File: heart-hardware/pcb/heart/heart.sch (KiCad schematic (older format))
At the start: 61 parts, among them J1 3V0, J2 DIO, J3 CLK, J4 GND, SW1 SW_SPDT, U1 STM32L031F6Px, U2 TCA6416APWR, U3 LIS3DH

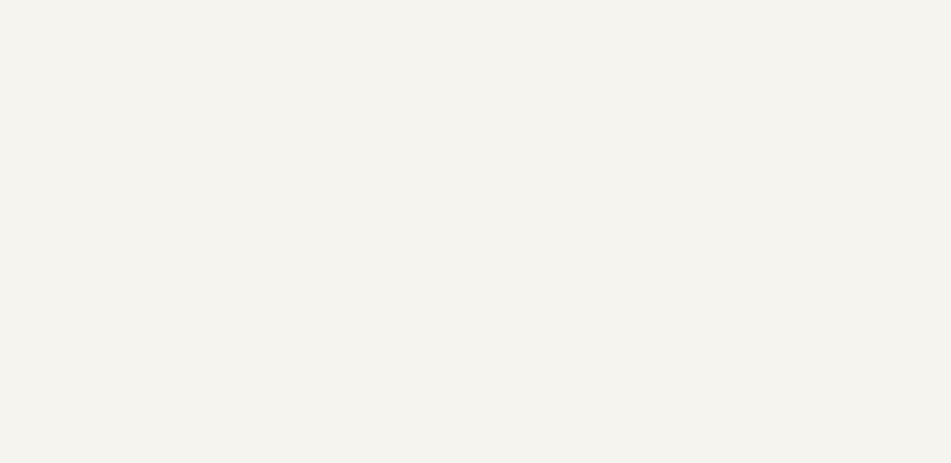
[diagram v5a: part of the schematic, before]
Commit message: Added touch key
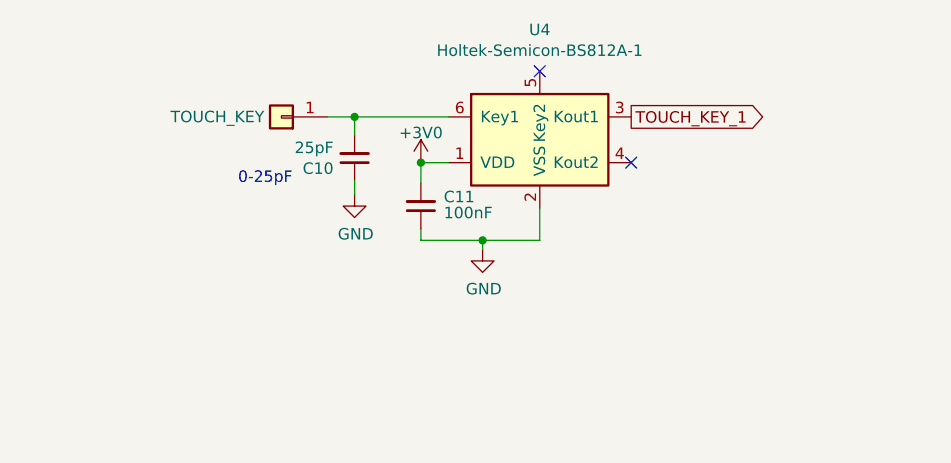
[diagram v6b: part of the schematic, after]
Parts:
- added C10: 25pF, Capacitor_SMD:C_0402_1005Metric, symbol Device:C_Small
- added C11: 100nF, Capacitor_SMD:C_0402_1005Metric, symbol Device:C_Small
- added J5: TOUCH_KEY, TestPoint:TestPoint_Pad_1.0x1.0mm, symbol Connector_Generic:Conn_01x01
- added U4: Holtek-Semicon-BS812A-1, Package_TO_SOT_SMD:SOT-23-6, symbol Sensor_Touch:Holtek-Semicon-BS812A-1
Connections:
- net +3V0: now also C11.2, U4.1 (VDD)
- net GND: now also C10.1, C11.1, U4.2 (VSS)
- new net: C10.2, J5.1 (Pin_1), U4.6 (Key1)
- new net TOUCH_KEY_1: U4.3 (Kout1)
- no-connect marks 10 -> 12
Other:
- note added: "0-25pF"
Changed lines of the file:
@@
 	1    0    0    -1
 $EndComp
+NoConn ~ 8720 1740
+NoConn ~ 8320 1340
+Text GLabel 8720 1540 2    50   Output ~ 0
+TOUCH_KEY_1
+Wire Wire Line
+	7800 2030 7800 2080
+Wire Wire Line
+	7800 2080 8070 2080
+Wire Wire Line
+	8320 2080 8320 1940
+Wire Wire Line
+	8070 2080 8070 2120
+Connection ~ 8070 2080
+Wire Wire Line
+	8070 2080 8320 2080
+$Comp
+L power:GND #PWR0128
+U 1 1 61CFF552
+P 8070 2120
+F 0 "#PWR0128" H 8070 1870 50  0001 C CNN
+F 1 "GND" H 8075 1947 50  0000 C CNN
+F 2 "" H 8070 2120 50  0001 C CNN
+F 3 "" H 8070 2120 50  0001 C CNN
+	1    8070 2120
+	1    0    0    -1
+$EndComp
+Wire Wire Line
+	7800 1830 7800 1740
+Wire Wire Line
+	7800 1740 7920 1740
+$Comp
+L power:+3V0 #PWR0129
+U 1 1 61D0AF5F
+P 7800 1740
+F 0 "#PWR0129" H 7800 1590 50  0001 C CNN
+F 1 "+3V0" H 7800 1870 50  0000 C CNN
+F 2 "" H 7800 1740 50  0001 C CNN
+F 3 "" H 7800 1740 50  0001 C CNN
+	1    7800 1740
+	1    0    0    -1
+$EndComp
+Connection ~ 7800 1740
+Wire Wire Line
+	7920 1540 7510 1540
+Wire Wire Line
+	7510 1540 7510 1620
+$Comp
+L power:GND #PWR0130
+U 1 1 61D23FB4
+P 7510 1880
+F 0 "#PWR0130" H 7510 1630 50  0001 C CNN
+F 1 "GND" H 7515 1707 50  0000 C CNN
+F 2 "" H 7510 1880 50  0001 C CNN
+F 3 "" H 7510 1880 50  0001 C CNN
+	1    7510 1880
+	1    0    0    -1
+$EndComp
+$Comp
+L Connector_Generic:Conn_01x01 J5
+U 1 1 61D2FEB8
+P 7190 1540
+F 0 "J5" H 7108 1315 50  0001 C CNN
+F 1 "TOUCH_KEY" H 7470 1540 50  0000 C CNN
+F 2 "TestPoint:TestPoint_Pad_1.0x1.0mm" H 7190 1540 50  0001 C CNN
+F 3 "~" H 7190 1540 50  0001 C CNN
+	1    7190 1540
+	-1   0    0    1
+$EndComp
+Wire Wire Line
+	7510 1540 7390 1540
+Connection ~ 7510 1540
+$Comp
+L Device:C_Small C11
+U 1 1 61D48188
+P 7800 1930
+F 0 "C11" H 7700 1890 50  0000 R CNN
+F 1 "100nF" H 7700 1960 50  0000 R CNN
+F 2 "Capacitor_SMD:C_0402_1005Metric" H 7800 1930 50  0001 C CNN
+F 3 "~" H 7800 1930 50  0001 C CNN
+	1    7800 1930
+	-1   0    0    1
+$EndComp
+$Comp
+L Sensor_Touch:Holtek-Semicon-BS812A-1 U4
+U 1 1 61CA1B9B
+P 8320 1640
+F 0 "U4" H 8320 2121 50  0000 C CNN
+F 1 "Holtek-Semicon-BS812A-1" H 8320 2030 50  0000 C CNN
+F 2 "Package_TO_SOT_SMD:SOT-23-6" H 8370 1940 50  0001 C CNN
+F 3 "" H 8370 1940 50  0001 C CNN
+	1    8320 1640
+	1    0    0    -1
+$EndComp
+$Comp
+L Device:C_Small C10
+U 1 1 61CC936F
+P 7510 1720
+F 0 "C10" H 7602 1766 50  0000 L CNN
+F 1 "25pF" H 7602 1675 50  0000 L CNN
+F 2 "Capacitor_SMD:C_0402_1005Metric" H 7510 1720 50  0001 C CNN
+F 3 "~" H 7510 1720 50  0001 C CNN
+	1    7510 1720
+	-1   0    0    1
+$EndComp
+Wire Wire Line
+	7510 1820 7510 1880
+Text Notes 7000 1840 0    50   ~ 0
+0-25pF
 $EndSCHEMATC

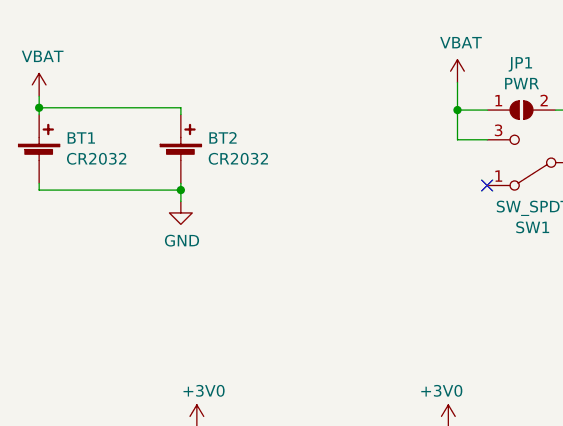
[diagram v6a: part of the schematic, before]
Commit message: Changed battery from 2x CR2032 to 1x CR2450
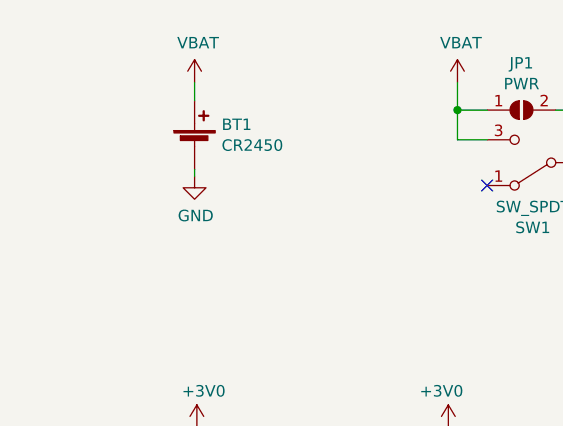
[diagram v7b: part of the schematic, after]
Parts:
- removed BT2: CR2032, Battery:BatteryHolder_Keystone_3034_1x20mm, symbol Device:Battery_Cell
- BT1: value CR2032 -> CR2450; footprint Battery:BatteryHolder_Keystone_3034_1x20mm -> Battery:BatteryHolder_Keystone_3008_1x2450
- J5: footprint TestPoint:TestPoint_Pad_1.0x1.0mm -> TestPoint:TestPoint_Pad_D4.0mm
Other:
- moved on the sheet: BT1
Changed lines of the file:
@@
 $EndDescr
-$Comp
-L Device:Battery_Cell BT2
-U 1 1 61C08941
-P 1630 1730
-F 0 "BT2" H 1748 1826 50  0000 L CNN
-F 1 "CR2032" H 1748 1735 50  0000 L CNN
-F 2 "Battery:BatteryHolder_Keystone_3034_1x20mm" V 1630 1790 50  0001 C CNN
-F 3 "~" V 1630 1790 50  0001 C CNN
-	1    1630 1730
-	1    0    0    -1
-$EndComp
-Wire Wire Line
-	1010 1860 1630 1860
 $Comp
 L power:GND #PWR0101
 U 1 1 61C0AAF9
-P 1630 1910
-F 0 "#PWR0101" H 1630 1660 50  0001 C CNN
-F 1 "GND" H 1635 1737 50  0000 C CNN
-F 2 "" H 1630 1910 50  0001 C CNN
-F 3 "" H 1630 1910 50  0001 C CNN
-	1    1630 1910
-	1    0    0    -1
-$EndComp
-Wire Wire Line
-	1630 1860 1630 1910
+P 1690 1800
+F 0 "#PWR0101" H 1690 1550 50  0001 C CNN
+F 1 "GND" H 1695 1627 50  0000 C CNN
+F 2 "" H 1690 1800 50  0001 C CNN
+F 3 "" H 1690 1800 50  0001 C CNN
+	1    1690 1800
+	1    0    0    -1
+$EndComp
 $Comp
 L Device:Battery_Cell BT1
 U 1 1 61BFD73A
-P 1010 1730
-F 0 "BT1" H 1128 1826 50  0000 L CNN
-F 1 "CR2032" H 1128 1735 50  0000 L CNN
-F 2 "Battery:BatteryHolder_Keystone_3034_1x20mm" V 1010 1790 50  0001 C CNN
-F 3 "~" V 1010 1790 50  0001 C CNN
-	1    1010 1730
-	1    0    0    -1
-$EndComp
-Wire Wire Line
-	1010 1500 1630 1500
-Wire Wire Line
-	1010 1500 1010 1450
+P 1690 1670
+F 0 "BT1" H 1808 1766 50  0000 L CNN
+F 1 "CR2450" H 1808 1675 50  0000 L CNN
+F 2 "Battery:BatteryHolder_Keystone_3008_1x2450" V 1690 1730 50  0001 C CNN
+F 3 "~" V 1690 1730 50  0001 C CNN
+	1    1690 1670
+	1    0    0    -1
+$EndComp
 $Comp
 L power:VBAT #PWR0102
 U 1 1 61C0CB09
-P 1010 1450
-F 0 "#PWR0102" H 1010 1300 50  0001 C CNN
-F 1 "VBAT" H 1025 1623 50  0000 C CNN
-F 2 "" H 1010 1450 50  0001 C CNN
-F 3 "" H 1010 1450 50  0001 C CNN
-	1    1010 1450
-	1    0    0    -1
-$EndComp
-Wire Wire Line
-	1010 1530 1010 1500
-Connection ~ 1010 1500
-Wire Wire Line
-	1010 1860 1010 1830
-Wire Wire Line
-	1630 1860 1630 1830
-Connection ~ 1630 1860
-Wire Wire Line
-	1630 1530 1630 1500
+P 1690 1390
+F 0 "#PWR0102" H 1690 1240 50  0001 C CNN
+F 1 "VBAT" H 1705 1563 50  0000 C CNN
+F 2 "" H 1690 1390 50  0001 C CNN
+F 3 "" H 1690 1390 50  0001 C CNN
+	1    1690 1390
+	1    0    0    -1
+$EndComp
+Wire Wire Line
+	1690 1800 1690 1770
 $Comp
 L power:VBAT #PWR0103
@@
 F 0 "J5" H 7108 1315 50  0001 C CNN
 F 1 "TOUCH_KEY" H 7470 1540 50  0000 C CNN
-F 2 "TestPoint:TestPoint_Pad_1.0x1.0mm" H 7190 1540 50  0001 C CNN
+F 2 "TestPoint:TestPoint_Pad_D4.0mm" H 7190 1540 50  0001 C CNN
 F 3 "~" H 7190 1540 50  0001 C CNN
 	1    7190 1540
@@
 Text Notes 7000 1840 0    50   ~ 0
 0-25pF
+Wire Wire Line
+	1690 1390 1690 1470
 $EndSCHEMATC

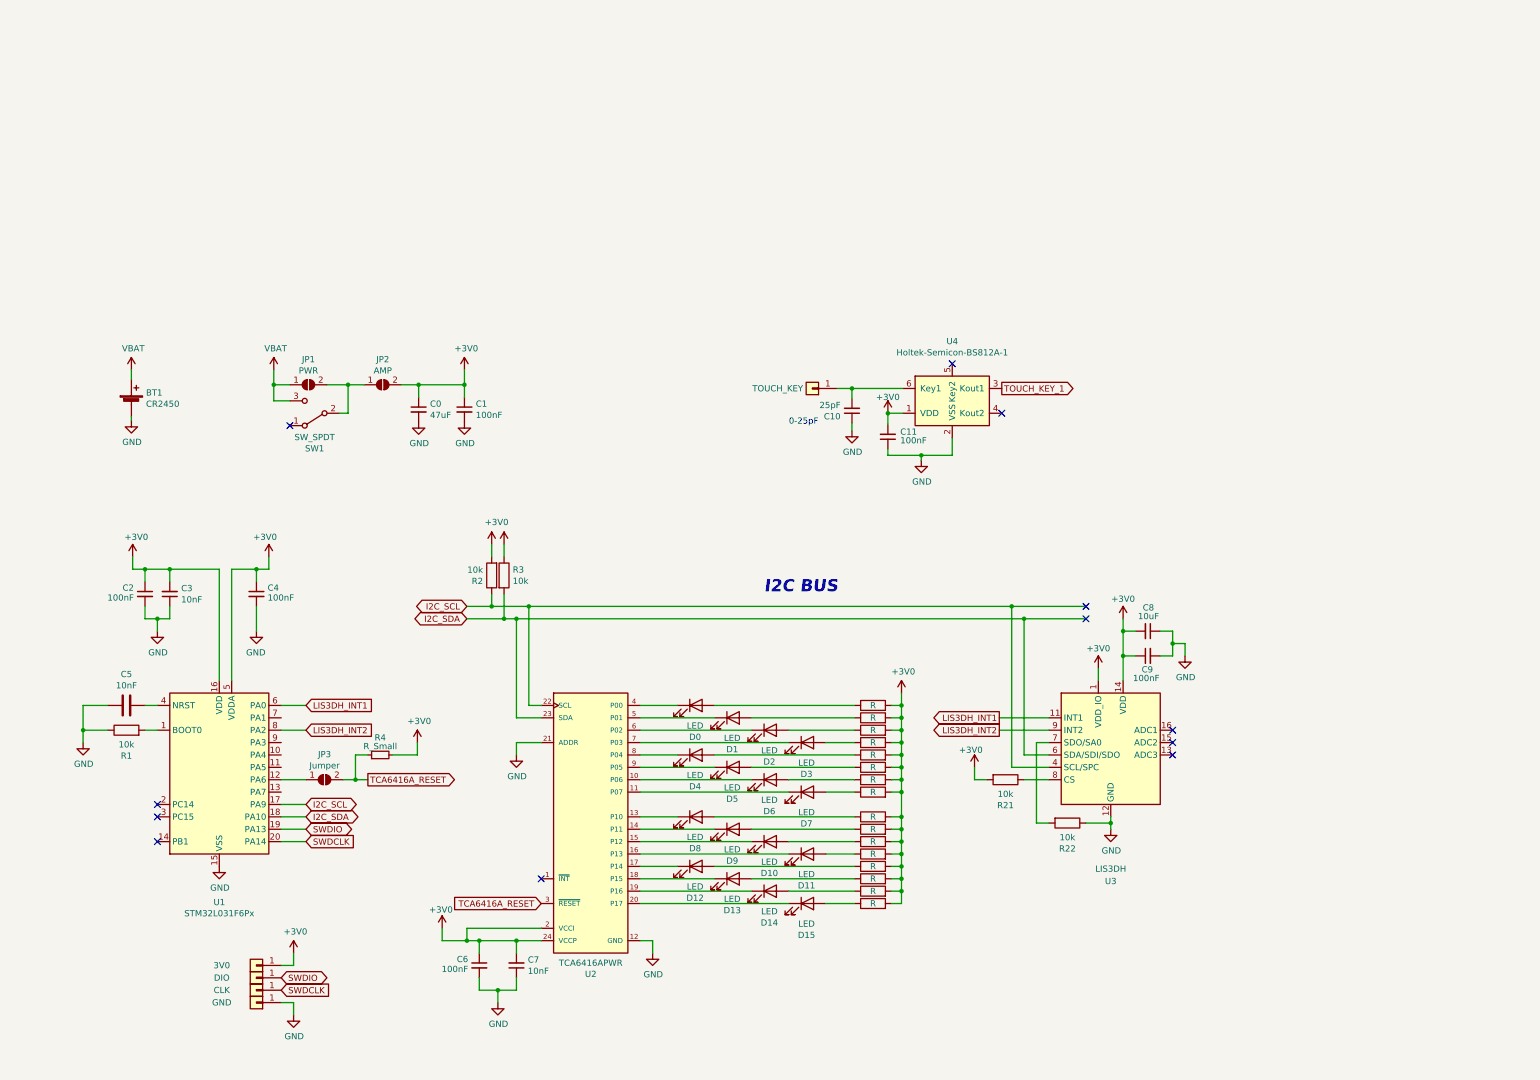
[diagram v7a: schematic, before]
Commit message: New heart shape, battery change, top layer component placed v1
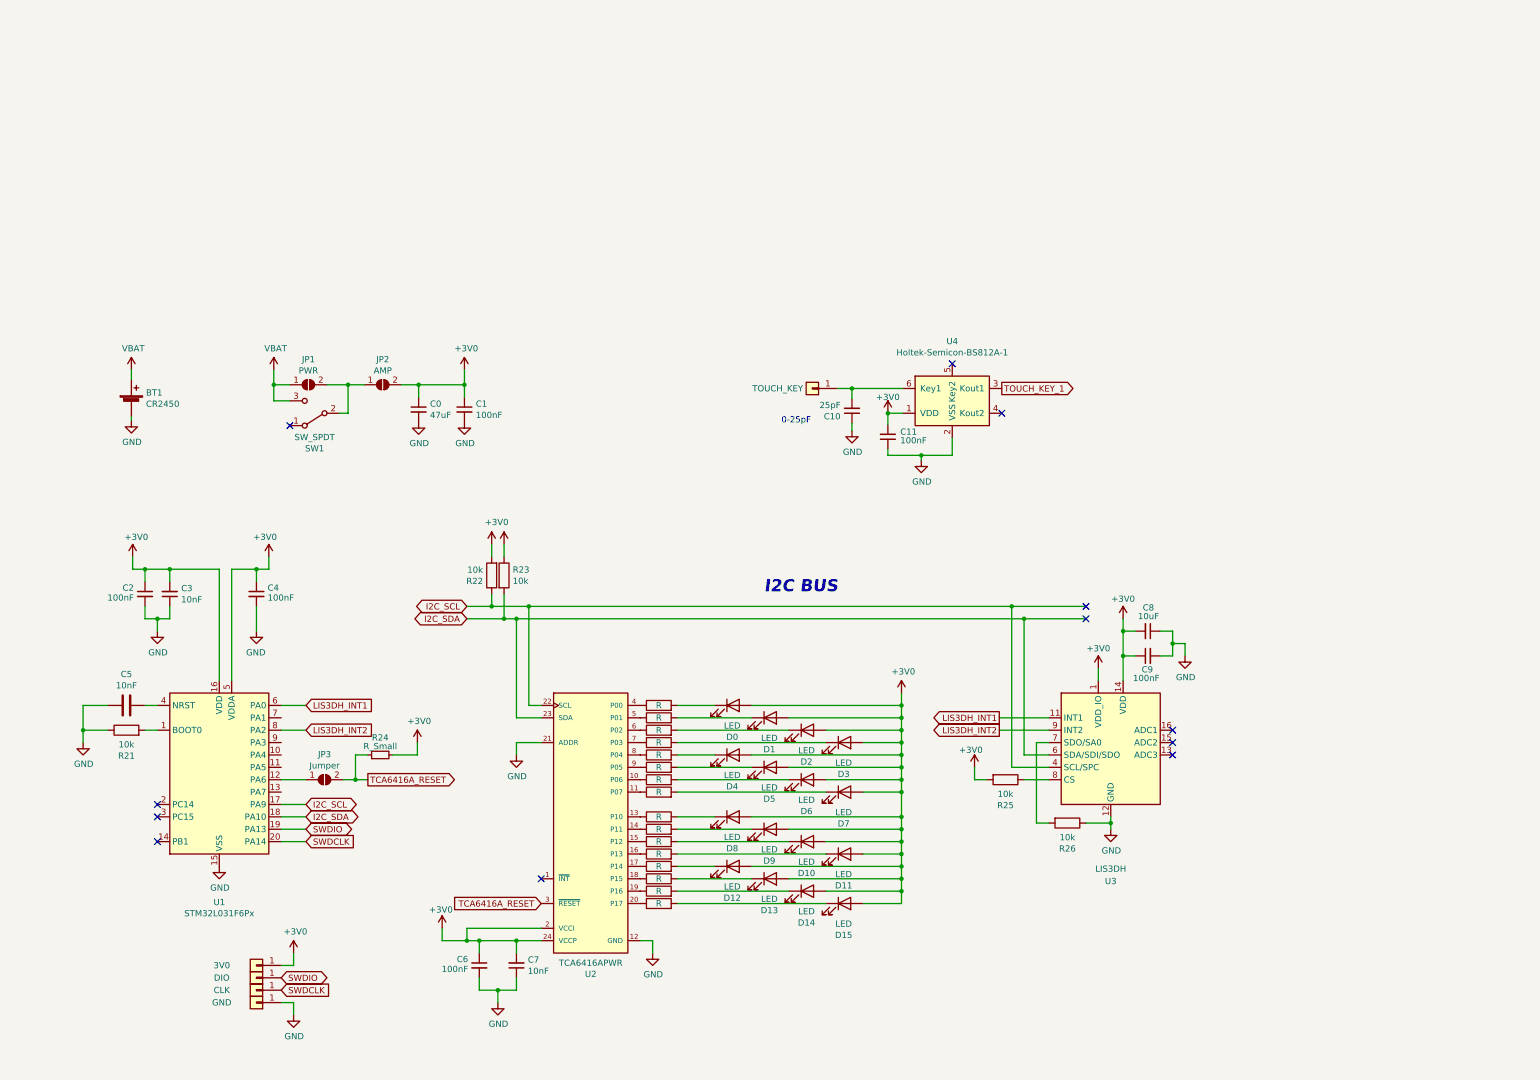
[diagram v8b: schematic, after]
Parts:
- renumbered R8 to R0, R7 to R1, R15 to R10, R16 to R11, R17 to R12, R18 to R13, R19 to R14, R20 to R15, R5 to R2, R1 to R21, R2 to R22, R3 to R23, R4 to R24, R21 to R25, R22 to R26, R6 to R3, R9 to R4, R10 to R5, R11 to R6, R12 to R7, R13 to R8, R14 to R9
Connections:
- net +3V0: now also D0.2 (A), D1.2 (A), D10.2 (A), D11.2 (A), D12.2 (A), D13.2 (A), D14.2 (A), D15.2 (A), D2.2 (A), D3.2 (A), D4.2 (A), D5.2 (A), D6.2 (A), D7.2 (A), D8.2 (A), D9.2 (A); no longer R0.2, R1.2, R10.2, R11.2, R12.2, R13.2, R14.2, R15.2, R2.2, R3.2, R4.2, R5.2, R6.2, R7.2, R8.2, R9.2
- net at U2.10 (P06): now also R6.1; no longer D6.1 (K)
- net at U2.11 (P07): now also R7.1; no longer D7.1 (K)
- net at U2.13 (P10): now also R8.1; no longer D8.1 (K)
- net at U2.14 (P11): now also R9.1; no longer D9.1 (K)
- net at U2.15 (P12): now also R10.1; no longer D10.1 (K)
- net at U2.16 (P13): now also R11.1; no longer D11.1 (K)
- net at U2.17 (P14): now also R12.1; no longer D12.1 (K)
- net at U2.18 (P15): now also R13.1; no longer D13.1 (K)
- net at U2.19 (P16): now also R14.1; no longer D14.1 (K)
- net at U2.20 (P17): now also R15.1; no longer D15.1 (K)
- net at U2.4 (P00): now also R0.1; no longer D0.1 (K)
- net at U2.5 (P01): now also R1.1; no longer D1.1 (K)
- net at U2.6 (P02): now also R2.1; no longer D2.1 (K)
- net at U2.7 (P03): now also R3.1; no longer D3.1 (K)
- net at U2.8 (P04): now also R4.1; no longer D4.1 (K)
- net at U2.9 (P05): now also R5.1; no longer D5.1 (K)
- new net: D1.1 (K), R1.2
- new net: D0.1 (K), R0.2
- new net: D7.1 (K), R7.2
- new net: D6.1 (K), R6.2
- new net: D5.1 (K), R5.2
- new net: D4.1 (K), R4.2
- new net: D3.1 (K), R3.2
- new net: D2.1 (K), R2.2
- new net: D11.1 (K), R11.2
- new net: D10.1 (K), R10.2
- new net: D9.1 (K), R9.2
- new net: D8.1 (K), R8.2
- new net: D15.1 (K), R15.2
- new net: D12.1 (K), R12.2
- new net: D13.1 (K), R13.2
- new net: D14.1 (K), R14.2
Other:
- moved on the sheet: D0, D1, D10, D11, D12, D13, D14, D15, D2, D3, D4, D5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
